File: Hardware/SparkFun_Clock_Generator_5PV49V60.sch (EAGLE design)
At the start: 27 parts, among them U1 IDT_5P49V60_CLOCK_GENERATOR, Y2 26MHZ

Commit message: Routes board
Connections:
- new net N$3: JP1.3, R1.1
- net SEL0/SCL: no longer JP1.3, R1.1
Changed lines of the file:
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@@
-</segment>
-<segment>
-<pinref part="JP1" gate="G$1" pin="3"/>
-<wire x1="134.62" y1="157.48" x2="132.08" y2="157.48" width="0.1524" layer="91"/>
-<wire x1="132.08" y1="157.48" x2="132.08" y2="152.4" width="0.1524" layer="91"/>
-<pinref part="R1" gate="G$1" pin="1"/>
-<wire x1="132.08" y1="152.4" x2="142.24" y2="152.4" width="0.1524" layer="91"/>
 </segment>
 <segment>
@@
 </segment>
 </net>
+<net name="N$3" class="0">
+<segment>
+<pinref part="R1" gate="G$1" pin="1"/>
+<wire x1="142.24" y1="152.4" x2="132.08" y2="152.4" width="0.1524" layer="91"/>
+<wire x1="132.08" y1="152.4" x2="132.08" y2="157.48" width="0.1524" layer="91"/>
+<pinref part="JP1" gate="G$1" pin="3"/>
+<wire x1="132.08" y1="157.48" x2="134.62" y2="157.48" width="0.1524" layer="91"/>
+</segment>
+</net>

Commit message: Adds silk, so much silk
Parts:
- removed Y2: 26MHZ, SparkFun-Clocks:CRYSTAL-26MHZSMD-3.2X2.5
- added C10, C12: 12pF, SparkFun-Capacitors:12PF-0402-50V-5%
- added D1: RED, SparkFun-LED:LED-RED0603
- added J5: TEST-POINTTP_15TH_THRU, SparkFun-Connectors:TEST-POINTTP_15TH_THRU
- added LED: JUMPER-SMT_2_NC_TRACE_SILK, SparkFun-Jumpers:JUMPER-SMT_2_NC_TRACE_SILK
- added LOGO1: SFE_LOGO_NAME_FLAME.1_INCH, SparkFun-Aesthetics:SFE_LOGO_NAME_FLAME.1_INCH
- added LOGO2: OSHW-LOGOS, SparkFun-Aesthetics:OSHW-LOGOS
- added LOGO3: QWIIC_LOGO_4MM, SparkFun-Aesthetics:QWIIC_LOGO_4MM
- added R3: 1KOHM-0402-1/16W-1%, SparkFun-Resistors:1KOHM-0402-1/16W-1%
- added Y1: 16MHz, SparkFun-Clocks:CRYSTAL-16MHZ_SMALL
- J3: device SparkFun-Connectors:CONN_063.5MM-6 -> SparkFun-Connectors:CONN_083.5MM-8
- J6: value (none) -> TEST-POINTTP_15TH_THRU; device SparkFun-Connectors:CONN_021X02_NO_SILK -> SparkFun-Connectors:TEST-POINTTP_15TH_THRU
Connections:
- new net N$5: D1.A, R3.1
- new net N$6: C10.1, U1.XIN, Y1.2
- net 3.3V: now also LED.2
- net CLKIN: now also J5.1; no longer J6.1
- net CLKINB: now also J6.1; no longer J6.2
- net GND: now also C10.2, C12.2, D1.C, Y1.GND; no longer Y2.3
- net N$2: now also C12.1, U1.XOUT, Y1.1; no longer U1.XIN, Y2.1
- net N$4: now also LED.1, R3.2; no longer U1.XOUT, Y2.2
- net OUT1: now also J3.8; no longer J3.6
- net OUT1B: now also J3.7; no longer J3.5
- net OUT2: now also J3.6; no longer J3.4
- net OUT2B: now also J3.5; no longer J3.3
- net OUT3: now also J3.4; no longer J3.2
- net OUT3B: now also J3.3; no longer J3.1
- net OUT4: now also J3.2
- net OUT4B: now also J3.1
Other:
- note added: "Clock Generator - 5P49V60"
- note added: "Decoupling Caps"
- note added: "Headers"
- note added: "Jumpers"
- note added: "Screw Terminal"
- moved on the sheet: C1, C2, C3, C4, C5, C6, C7, C8, C9, FB1, J1, J2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

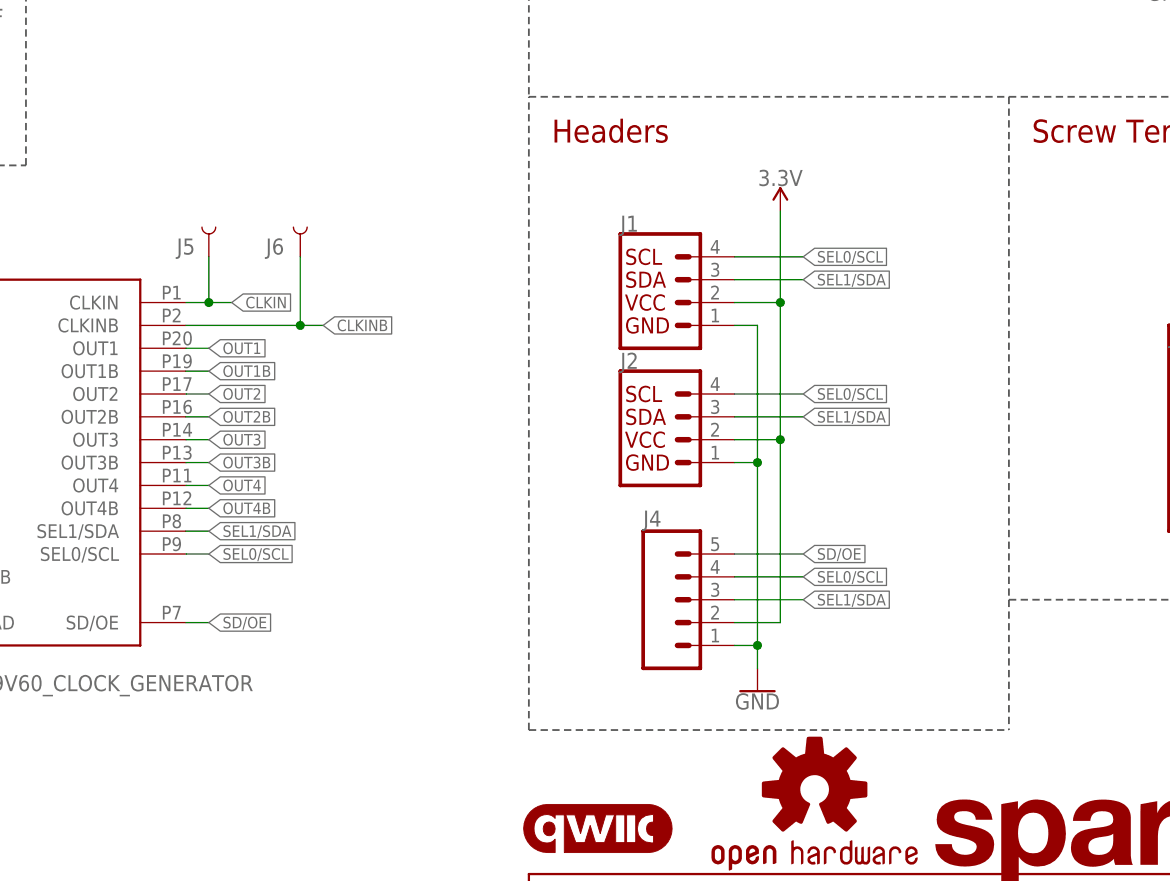
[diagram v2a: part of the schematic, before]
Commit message: Adds silk to jumpers and adds smaller diameter through holes for clock signals
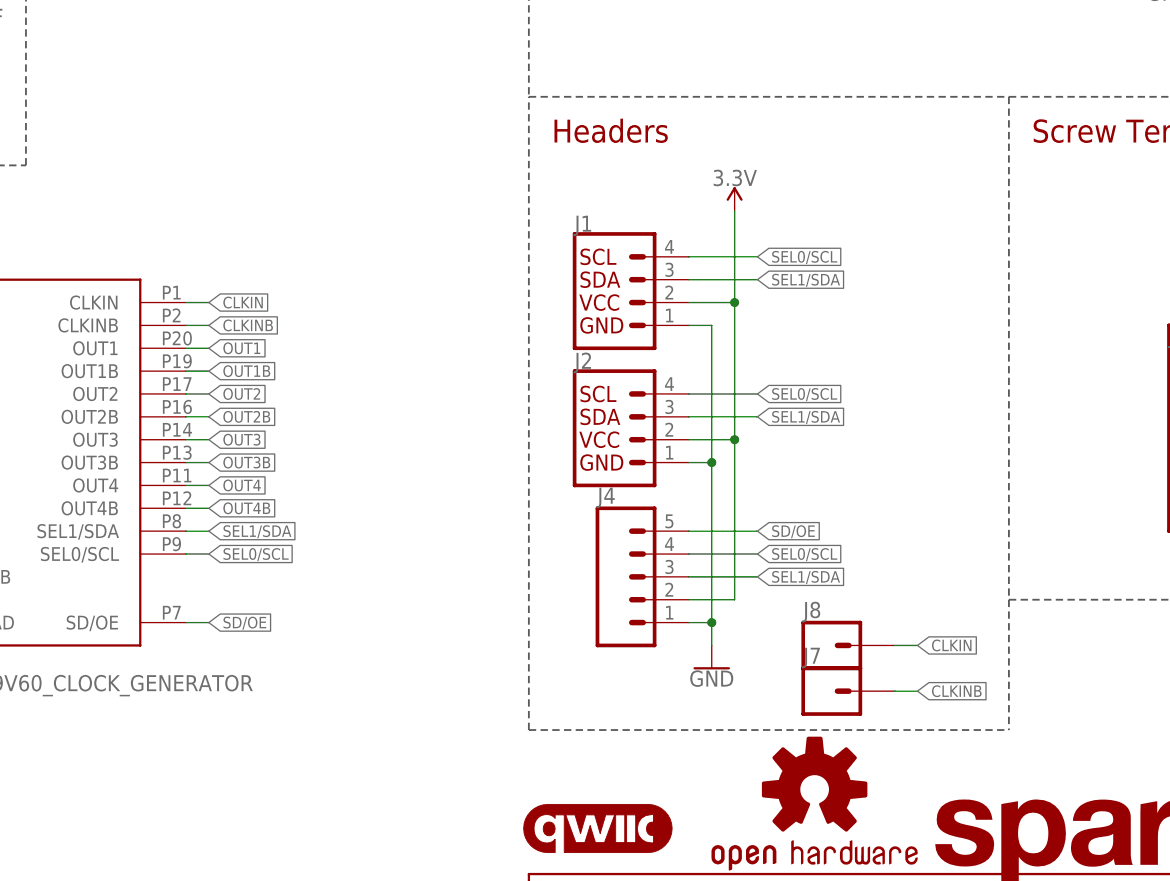
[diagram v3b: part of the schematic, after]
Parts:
- removed J5, J6: TEST-POINTTP_15TH_THRU, SparkFun-Connectors:TEST-POINTTP_15TH_THRU
- added J7, J8: (no value), SparkFun-Connectors:CONN_01PTH_NO_SILK_SMALL
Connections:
- net CLKIN: now also J8.1; no longer J5.1
- net CLKINB: now also J7.1; no longer J6.1
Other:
- moved on the sheet: J1, J2, J4

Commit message: Minor adjustments to schematic
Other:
- note added: "Cut to disable Power LED"
- note added: "Cut to remove I2C Pullup Resistors"
- note added: "VCC Range: 1.71 - 3.465V"
- moved on the sheet: C7, C8, J3

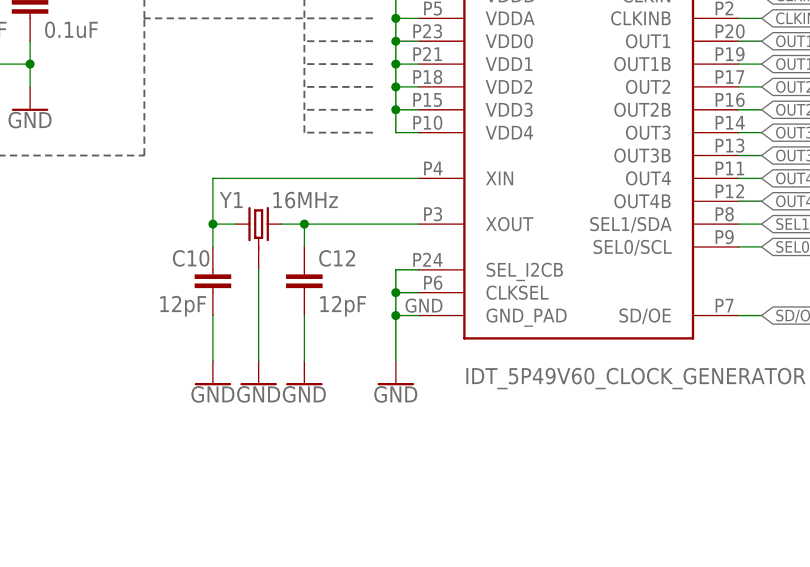
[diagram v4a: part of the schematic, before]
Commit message: Removes pulling SEL_I2CB line from ground, and instead leaves it floating
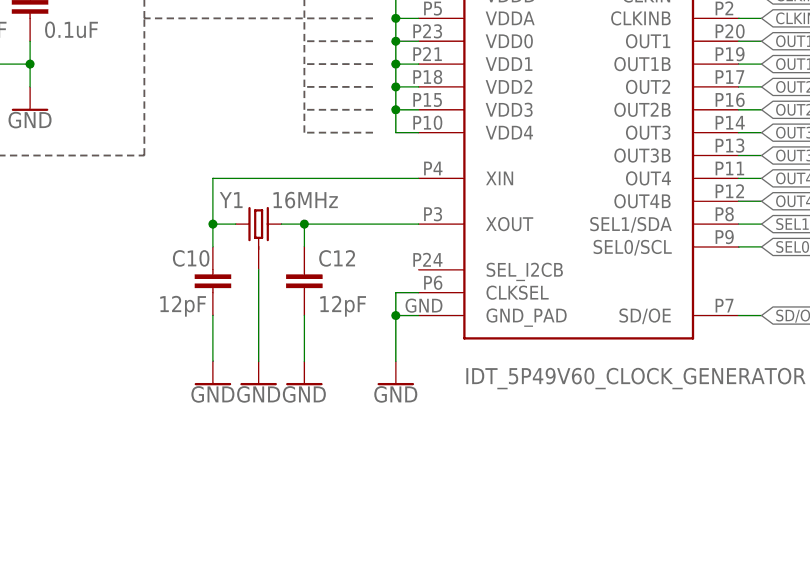
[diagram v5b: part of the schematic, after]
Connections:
- net GND: no longer U1.SEL_I2CB
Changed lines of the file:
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@@
 <wire x1="71.12" y1="66.04" x2="71.12" y2="63.5" width="0.1524" layer="91"/>
 <wire x1="73.66" y1="66.04" x2="71.12" y2="66.04" width="0.1524" layer="91"/>
-<pinref part="U1" gate="G$1" pin="SEL_I2CB"/>
-<wire x1="73.66" y1="68.58" x2="71.12" y2="68.58" width="0.1524" layer="91"/>
-<wire x1="71.12" y1="66.04" x2="71.12" y2="68.58" width="0.1524" layer="91"/>
-<junction x="71.12" y="66.04"/>
 </segment>
 <segment>

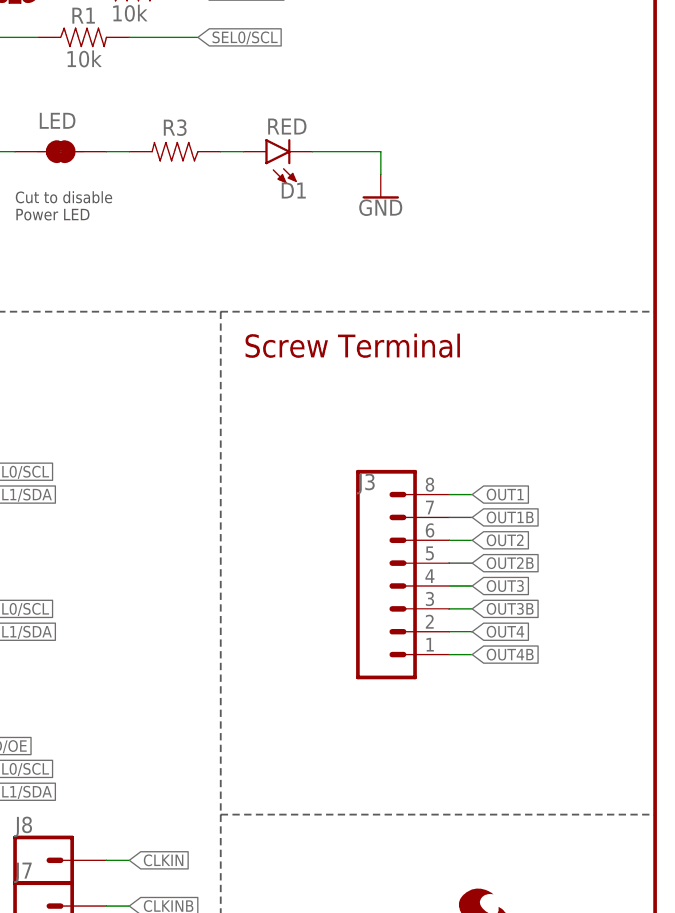
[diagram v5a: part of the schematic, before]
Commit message: Removes screw terminals in place of PTH header (with additional ground through holes)
* Adds better silk that...just makes more sense
* Adds ground vias to ground pad under IC
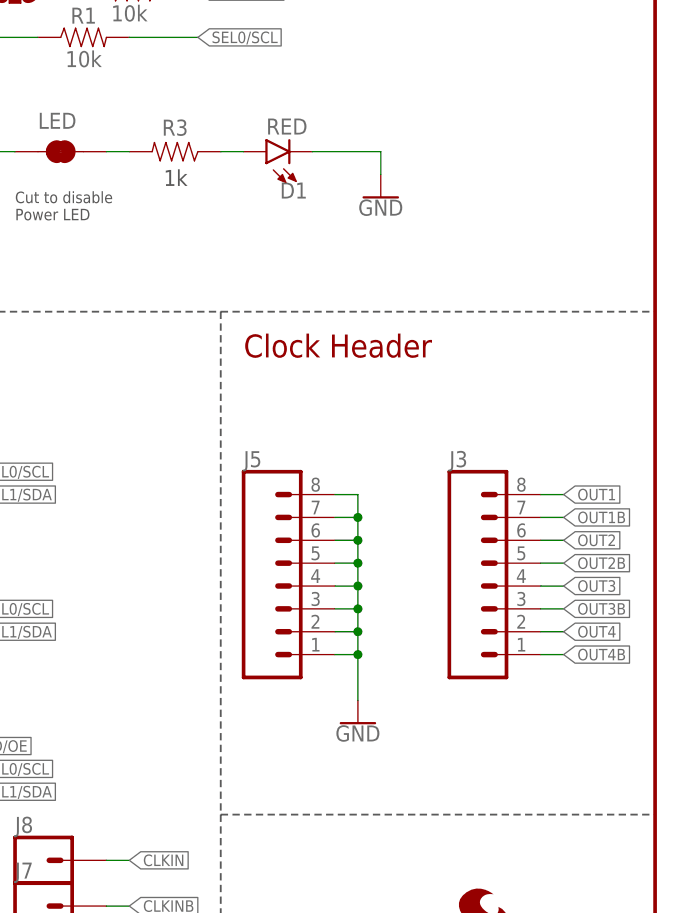
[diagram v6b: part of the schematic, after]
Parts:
- added J5: (no value), SparkFun-Connectors:CONN_08NO_SILK_FEMALE_PTH
- J3: device SparkFun-Connectors:CONN_083.5MM-8 -> SparkFun-Connectors:CONN_08NO_SILK_FEMALE_PTH
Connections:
- net GND: now also J5.1, J5.2, J5.3, J5.4, J5.5, J5.6, J5.7, J5.8
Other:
- note added: "1k"
- note added: "Clock Header"
- note removed: "Screw Terminal"
- moved on the sheet: J3
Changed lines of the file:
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@@
 <part name="SUPPLY2" library="SparkFun-PowerSymbols" deviceset="3.3V" device=""/>
 <part name="GND2" library="SparkFun-PowerSymbols" deviceset="GND" device=""/>
-<part name="J3" library="SparkFun-Connectors" deviceset="CONN_08" device="3.5MM-8"/>
 <part name="J4" library="SparkFun-Connectors" deviceset="CONN_05" device="NO_SILK"/>
 <part name="H1" library="SparkFun-Hardware" deviceset="STAND-OFF" device="TIGHT"/>
@@
 <part name="J7" library="SparkFun-Connectors" deviceset="CONN_01" device="PTH_NO_SILK_SMALL"/>
 <part name="J8" library="SparkFun-Connectors" deviceset="CONN_01" device="PTH_NO_SILK_SMALL"/>
+<part name="J3" library="SparkFun-Connectors" deviceset="CONN_08" device="NO_SILK_FEMALE_PTH"/>
+<part name="J5" library="SparkFun-Connectors" deviceset="CONN_08" device="NO_SILK_FEMALE_PTH"/>
+<part name="GND9" library="SparkFun-PowerSymbols" deviceset="GND" device=""/>
 </parts>
 <sheets>
@@
 <text x="152.4" y="177.8" size="2.54" layer="94" font="vector">Jumpers</text>
 <text x="149.86" y="116.84" size="2.54" layer="94" font="vector">Headers</text>
-<text x="203.2" y="116.84" size="2.54" layer="94" font="vector">Screw Terminal</text>
+<text x="203.2" y="116.84" size="2.54" layer="94" font="vector">Clock Header</text>
 <text x="17.78" y="149.86" size="2.54" layer="94" font="vector">Decoupling Caps</text>
 <wire x1="147.32" y1="51.562" x2="147.32" y2="121.92" width="0.2032" layer="97" style="shortdash"/>
@@
 Power LED</text>
 <text x="76.2" y="106.68" size="1.778" layer="97" font="vector">VCC Range: 1.71 - 3.465V</text>
+<text x="194.31" y="135.89" size="1.778" layer="97" font="vector">1k</text>
 </plain>
 <instances>
@@
 <attribute name="VALUE" x="167.64" y="58.166" size="1.778" layer="96" align="top-center"/>
 </instance>
-<instance part="J3" gate="G$1" x="220.98" y="91.44" smashed="yes">
-<attribute name="VALUE" x="215.9" y="81.534" size="1.778" layer="96" font="vector"/>
-<attribute name="NAME" x="215.9" y="102.108" size="1.778" layer="95" font="vector"/>
-</instance>
 <instance part="J4" gate="G$1" x="157.48" y="68.58" smashed="yes">
 <attribute name="VALUE" x="154.94" y="58.674" size="1.778" layer="96" font="vector"/>
@@
 <attribute name="VALUE" x="177.8" y="56.134" size="1.778" layer="96" font="vector"/>
 <attribute name="NAME" x="177.8" y="64.008" size="1.778" layer="95" font="vector"/>
+</instance>
+<instance part="J3" gate="G$1" x="231.14" y="91.44" smashed="yes">
+<attribute name="VALUE" x="226.06" y="78.994" size="1.778" layer="96" font="vector"/>
+<attribute name="NAME" x="226.06" y="104.648" size="1.778" layer="95" font="vector"/>
+</instance>
+<instance part="J5" gate="G$1" x="208.28" y="91.44" smashed="yes">
+<attribute name="VALUE" x="203.2" y="78.994" size="1.778" layer="96" font="vector"/>
+<attribute name="NAME" x="203.2" y="104.648" size="1.778" layer="95" font="vector"/>
+</instance>
+<instance part="GND9" gate="1" x="215.9" y="76.2" smashed="yes">
+<attribute name="VALUE" x="215.9" y="75.946" size="1.778" layer="96" align="top-center"/>
 </instance>
 </instances>
@@
 <wire x1="218.44" y1="139.7" x2="218.44" y2="137.16" width="0.1524" layer="91"/>
 </segment>
+<segment>
+<pinref part="J5" gate="G$1" pin="8"/>
+<wire x1="213.36" y1="101.6" x2="215.9" y2="101.6" width="0.1524" layer="91"/>
+<wire x1="215.9" y1="101.6" x2="215.9" y2="99.06" width="0.1524" layer="91"/>
+<pinref part="GND9" gate="1" pin="GND"/>
+<pinref part="J5" gate="G$1" pin="7"/>
+<wire x1="215.9" y1="99.06" x2="215.9" y2="96.52" width="0.1524" layer="91"/>
+<wire x1="215.9" y1="96.52" x2="215.9" y2="93.98" width="0.1524" layer="91"/>
+<wire x1="215.9" y1="93.98" x2="215.9" y2="91.44" width="0.1524" layer="91"/>
+<wire x1="215.9" y1="91.44" x2="215.9" y2="88.9" width="0.1524" layer="91"/>
+<wire x1="215.9" y1="88.9" x2="215.9" y2="86.36" width="0.1524" layer="91"/>
+<wire x1="215.9" y1="86.36" x2="215.9" y2="83.82" width="0.1524" layer="91"/>
+<wire x1="215.9" y1="83.82" x2="215.9" y2="78.74" width="0.1524" layer="91"/>
+<wire x1="213.36" y1="99.06" x2="215.9" y2="99.06" width="0.1524" layer="91"/>
+<junction x="215.9" y="99.06"/>
+<pinref part="J5" gate="G$1" pin="6"/>
+<wire x1="213.36" y1="96.52" x2="215.9" y2="96.52" width="0.1524" layer="91"/>
+<junction x="215.9" y="96.52"/>
+<pinref part="J5" gate="G$1" pin="5"/>
+<wire x1="213.36" y1="93.98" x2="215.9" y2="93.98" width="0.1524" layer="91"/>
+<junction x="215.9" y="93.98"/>
+<pinref part="J5" gate="G$1" pin="4"/>
+<wire x1="213.36" y1="91.44" x2="215.9" y2="91.44" width="0.1524" layer="91"/>
+<junction x="215.9" y="91.44"/>
+<pinref part="J5" gate="G$1" pin="3"/>
+<wire x1="213.36" y1="88.9" x2="215.9" y2="88.9" width="0.1524" layer="91"/>
+<junction x="215.9" y="88.9"/>
+<pinref part="J5" gate="G$1" pin="2"/>
+<wire x1="213.36" y1="86.36" x2="215.9" y2="86.36" width="0.1524" layer="91"/>
+<junction x="215.9" y="86.36"/>
+<pinref part="J5" gate="G$1" pin="1"/>
+<wire x1="213.36" y1="83.82" x2="215.9" y2="83.82" width="0.1524" layer="91"/>
+<junction x="215.9" y="83.82"/>
+</segment>
 </net>
 <net name="3.3V" class="0">
@@
 </segment>
 <segment>
+<wire x1="236.22" y1="101.6" x2="238.76" y2="101.6" width="0.1524" layer="91"/>
+<label x="238.76" y="101.6" size="1.27" layer="95" xref="yes"/>
 <pinref part="J3" gate="G$1" pin="8"/>
-<wire x1="226.06" y1="101.6" x2="228.6" y2="101.6" width="0.1524" layer="91"/>
-<label x="228.6" y="101.6" size="1.27" layer="95" xref="yes"/>
 </segment>
 </net>
@@
 </segment>
 <segment>
+<wire x1="236.22" y1="99.06" x2="238.76" y2="99.06" width="0.1524" layer="91"/>
+<label x="238.76" y="99.06" size="1.27" layer="95" xref="yes"/>
 <pinref part="J3" gate="G$1" pin="7"/>
-<wire x1="226.06" y1="99.06" x2="228.6" y2="99.06" width="0.1524" layer="91"/>
-<label x="228.6" y="99.06" size="1.27" layer="95" xref="yes"/>
 </segment>
 </net>
@@
 </segment>
 <segment>
+<wire x1="236.22" y1="96.52" x2="238.76" y2="96.52" width="0.1524" layer="91"/>
+<label x="238.76" y="96.52" size="1.27" layer="95" font="vector" xref="yes"/>
 <pinref part="J3" gate="G$1" pin="6"/>
-<wire x1="226.06" y1="96.52" x2="228.6" y2="96.52" width="0.1524" layer="91"/>
-<label x="228.6" y="96.52" size="1.27" layer="95" font="vector" xref="yes"/>
 </segment>
 </net>
@@
 </segment>
 <segment>
+<wire x1="236.22" y1="93.98" x2="238.76" y2="93.98" width="0.1524" layer="91"/>
+<label x="238.76" y="93.98" size="1.27" layer="95" font="vector" xref="yes"/>
 <pinref part="J3" gate="G$1" pin="5"/>
-<wire x1="226.06" y1="93.98" x2="228.6" y2="93.98" width="0.1524" layer="91"/>
-<label x="228.6" y="93.98" size="1.27" layer="95" font="vector" xref="yes"/>
 </segment>
 </net>
@@
 </segment>
 <segment>
+<wire x1="236.22" y1="91.44" x2="238.76" y2="91.44" width="0.1524" layer="91"/>
+<label x="238.76" y="91.44" size="1.27" layer="95" font="vector" xref="yes"/>
 <pinref part="J3" gate="G$1" pin="4"/>
-<wire x1="226.06" y1="91.44" x2="228.6" y2="91.44" width="0.1524" layer="91"/>
-<label x="228.6" y="91.44" size="1.27" layer="95" font="vector" xref="yes"/>
 </segment>
 </net>
@@
 </segment>
 <segment>
+<wire x1="236.22" y1="88.9" x2="238.76" y2="88.9" width="0.1524" layer="91"/>
+<label x="238.76" y="88.9" size="1.27" layer="95" font="vector" xref="yes"/>
 <pinref part="J3" gate="G$1" pin="3"/>
-<wire x1="226.06" y1="88.9" x2="228.6" y2="88.9" width="0.1524" layer="91"/>
-<label x="228.6" y="88.9" size="1.27" layer="95" font="vector" xref="yes"/>
 </segment>
 </net>
@@
 </segment>
 <segment>
+<wire x1="236.22" y1="86.36" x2="238.76" y2="86.36" width="0.1524" layer="91"/>
+<label x="238.76" y="86.36" size="1.27" layer="95" font="vector" xref="yes"/>
 <pinref part="J3" gate="G$1" pin="2"/>
-<wire x1="226.06" y1="86.36" x2="228.6" y2="86.36" width="0.1524" layer="91"/>
-<label x="228.6" y="86.36" size="1.27" layer="95" font="vector" xref="yes"/>
 </segment>
 </net>
@@
 </segment>
 <segment>
+<wire x1="236.22" y1="83.82" x2="238.76" y2="83.82" width="0.1524" layer="91"/>
+<label x="238.76" y="83.82" size="1.27" layer="95" font="vector" xref="yes"/>
 <pinref part="J3" gate="G$1" pin="1"/>
-<wire x1="226.06" y1="83.82" x2="228.6" y2="83.82" width="0.1524" layer="91"/>
-<label x="228.6" y="83.82" size="1.27" layer="95" font="vector" xref="yes"/>
-</segment>
-</net>
+</segment>
+</net>
